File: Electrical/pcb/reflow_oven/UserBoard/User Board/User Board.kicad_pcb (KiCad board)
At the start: 2 copper layers, 92.6 x 124.7 mm, 27 parts, among them J1 USER BOARD DISPLAY, J2 USER BOARD BUTTON, Q1 DMN13H750S, SW1 UP, SW2 LT, SW3 DWN, SW4 RT, SW5 OK

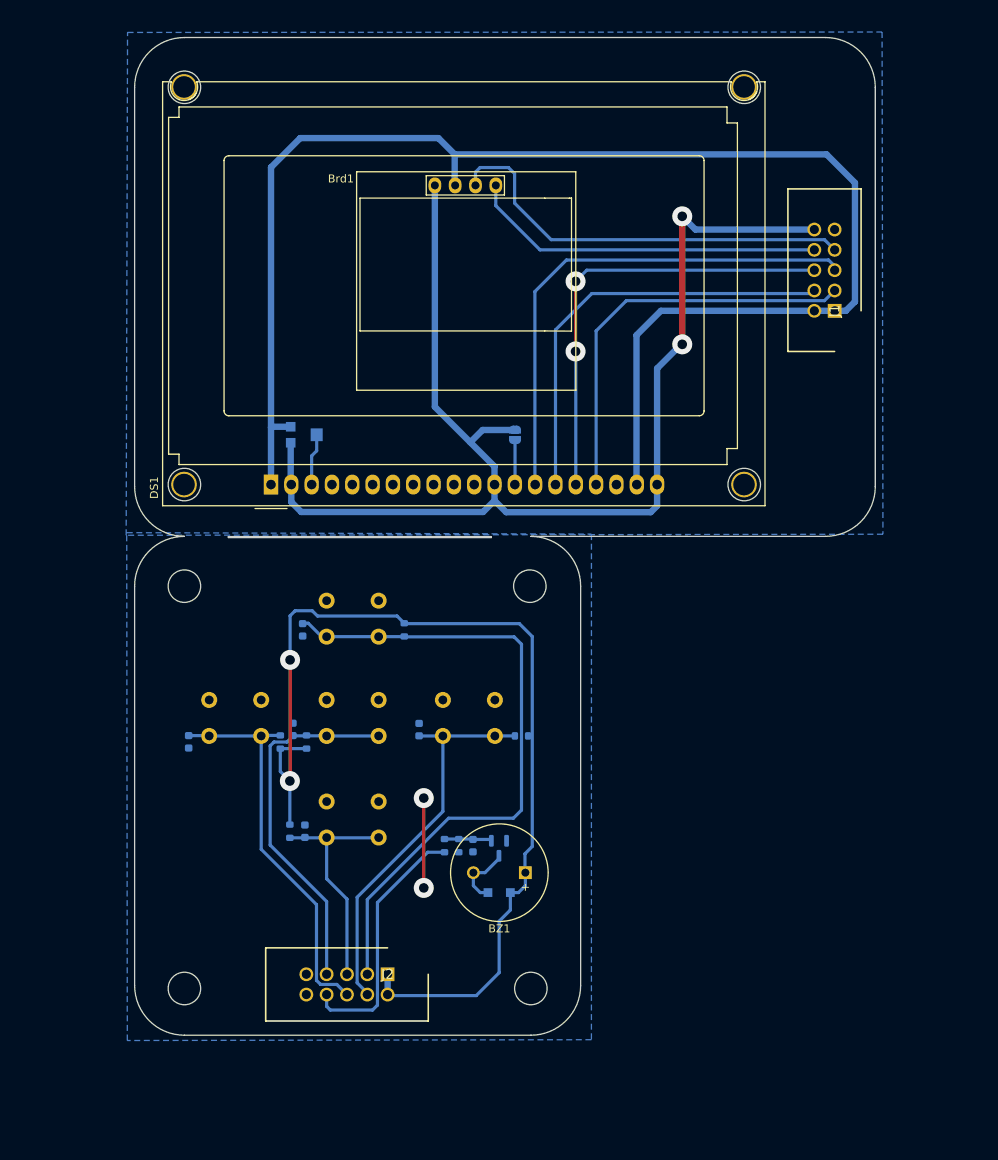
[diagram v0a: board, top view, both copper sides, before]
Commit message: fix
changed display footprint
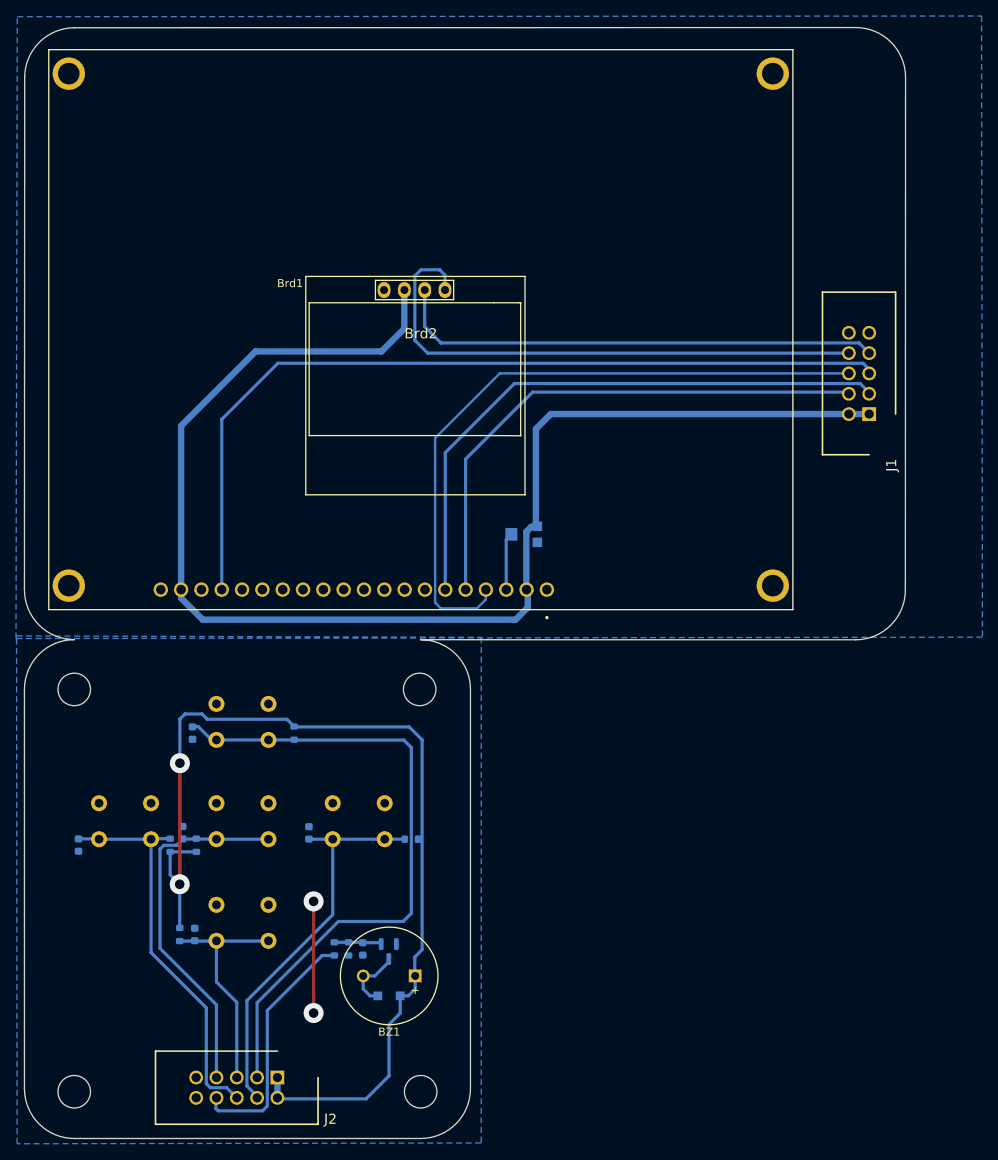
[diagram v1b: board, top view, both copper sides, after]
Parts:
- removed DS1: AG12864E, Display:AG12864E
- removed JP1: SolderJumper_2_Open, Jumper:SolderJumper-2_P1.3mm_Open_RoundedPad1.0x1.5mm
- added Brd2: 12864 LCD, footprint_lib:NHD12864AZFSWGBWVZ, F.Cu at (160.4, 100.9)
- moved RV1 30.1 mm to (157.5, 94.0), turned to -90 degrees
- moved SW2 18.9 mm to (140.1, 127.6)
- moved SW3 18.9 mm to (125.6, 140.3)
- moved SW5 18.9 mm to (125.6, 127.6)
- moved BZ1 18.9 mm to (143.9, 149.2)
- moved C1 18.9 mm to (137.4, 145.8)
- moved C3 18.9 mm to (130.6, 131.3)
- moved C5 18.9 mm to (101.8, 132.8)
- moved D1 18.9 mm to (140.6, 151.7)
- moved R1 18.9 mm to (133.8, 145.8)
- moved R2 18.9 mm to (135.6, 145.8)
- moved R7 18.9 mm to (116.6, 132.8)
- moved SW1 18.9 mm to (125.6, 115.2)
- moved SW4 18.9 mm to (110.9, 127.6)
- moved R3 18.9 mm to (128.8, 118.8)
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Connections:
- RV1 pad 1: GND -> +3V3
- RV1 pad 3: +3V3 -> GND
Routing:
- net GND: track 169.7 -> 14.0 mm, vias 4 -> 2
- net /LCD_RST: track 63.5 -> 105.4 mm
- net /LCD_CS: track 55.8 -> 83.9 mm, vias 2 -> 0
- net /I2C_SDA: track 44.6 -> 69.2 mm
- net /LCD_CLK: track 51.1 -> 74.1 mm
- net +3V3: track 313.5 -> 297.8 mm
- net /LCD_RW: track 53.2 -> 67.5 mm
- net /I2C_SCL: track 53.2 -> 61.5 mm
- net Net-(DS1-Pad13): track 5.53 -> 0.00 mm
- net Net-(BZ1-Pad2): track 8.76 -> 7.73 mm
- net /BUZZER: track 32.1 -> 31.3 mm
- net /UP_BTN: track 82.5 -> 81.8 mm
- net Net-(Brd2-Pad3): track 6.48 -> 7.18 mm
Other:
- board size 92.6 x 124.7 mm -> 110.1 x 138.9 mm

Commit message: user board
user board fab file
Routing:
- net /LCD_CS: track 83.9 -> 85.5 mm
- net +3V3: track 297.8 -> 298.9 mm
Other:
- outline, holes or cut-outs redrawn
